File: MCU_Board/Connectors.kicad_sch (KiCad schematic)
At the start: 6 parts, among them J1 Conn_ARM_JTAG_SWD_20, J2 USB_B_Micro, J3 Conn_02x05_Counter_Clockwise

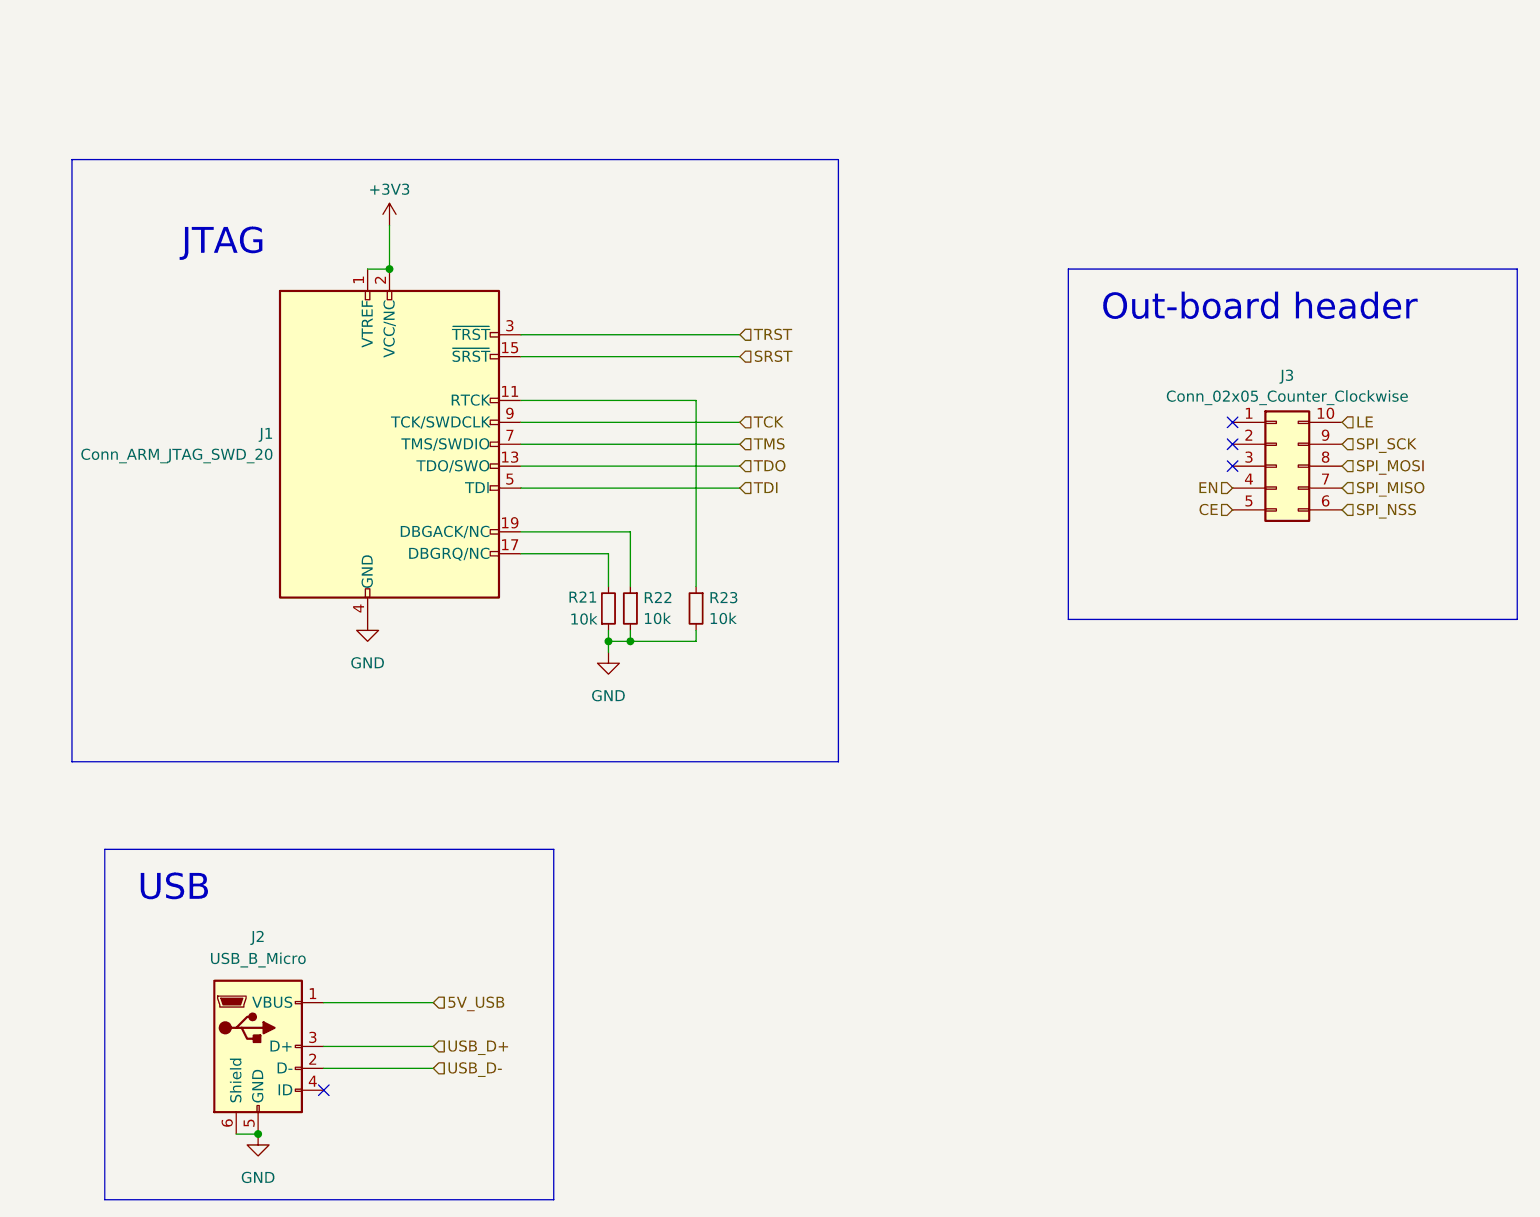
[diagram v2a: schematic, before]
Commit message: Finished MCU board
Finished MCU board and started finishing up the VCO board
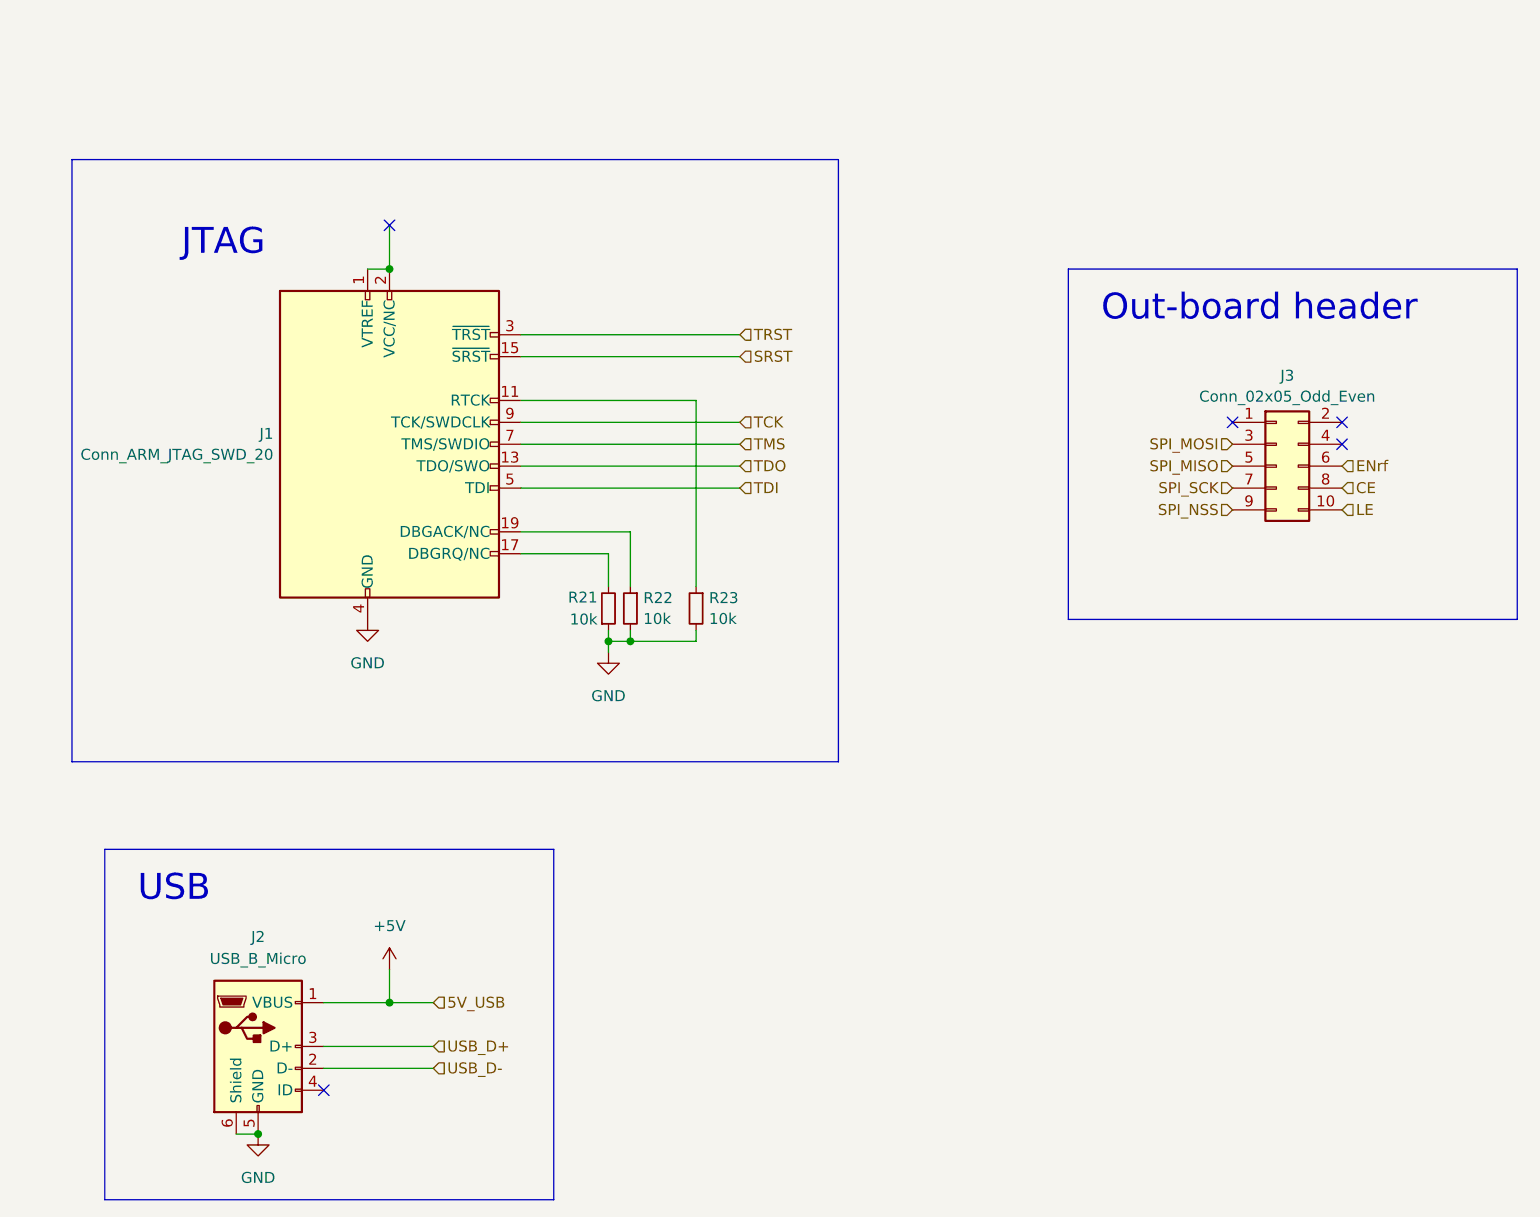
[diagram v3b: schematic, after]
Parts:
- removed J3: Conn_02x05_Counter_Clockwise, Connector_PinHeader_2.54mm:PinHeader_2x05_P2.54mm_Vertical, symbol Connector_Generic:Conn_02x05_Counter_Clockwise
- added J3: Conn_02x05_Odd_Even, Connector_PinHeader_2.54mm:PinHeader_2x05_P2.54mm_Vertical, symbol Connector_Generic:Conn_02x05_Odd_Even
- R21, R22, R23: footprint Resistor_SMD:R_0603_1608Metric_Pad0.98x0.95mm_HandSolder -> Resistor_SMD:R_0402_1005Metric_Pad0.72x0.64mm_HandSolder
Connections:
- net CE: now also J3.8 (Pin_8)
- net LE: now also J3.10 (Pin_10)
- net SPI_MISO: now also J3.5 (Pin_5)
- net SPI_MOSI: now also J3.3 (Pin_3)
- net SPI_NSS: now also J3.9 (Pin_9)
- net SPI_SCK: now also J3.7 (Pin_7)
- net +3V3: no longer names the net of J1.1 (VTREF), J1.2 (VCC/NC)
- net 5V_USB renamed +5V
- new net ENrf: J3.6 (Pin_6)
- no-connect marks 4 -> 5
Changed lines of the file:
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@@
   (junction (at 64.77 148.59) (diameter 0) (color 0 0 0 0)
   )
+  (junction (at 80.01 133.35) (diameter 0) (color 0 0 0 0)
+  )
   (junction (at 107.95 91.44) (diameter 0) (color 0 0 0 0)
   )
   (junction (at 80.01 48.26) (diameter 0) (color 0 0 0 0)
   )
-  (no_connect (at 177.8 71.12))
+  (no_connect (at 190.5 66.04))
+  (no_connect (at 190.5 68.58))
+  (no_connect (at 80.01 43.18))
   (no_connect (at 177.8 66.04))
-  (no_connect (at 177.8 68.58))
   (no_connect (at 72.39 143.51))
   (wire (pts (xy 85.09 140.97) (xy 72.39 140.97))
@@
     (stroke (width 0) (type default))
   )
+  (wire (pts (xy 80.01 129.54) (xy 80.01 133.35))
+    (stroke (width 0) (type default))
+  )
   (wire (pts (xy 95.25 63.5) (xy 115.57 63.5))
     (stroke (width 0) (type default))
@@
     (stroke (width 0) (type default))
   )
-  (wire (pts (xy 85.09 133.35) (xy 72.39 133.35))
+  (wire (pts (xy 85.09 133.35) (xy 80.01 133.35))
     (stroke (width 0) (type default))
   )
   (wire (pts (xy 115.57 63.5) (xy 115.57 85.09))
+    (stroke (width 0) (type default))
+  )
+  (wire (pts (xy 80.01 133.35) (xy 72.39 133.35))
     (stroke (width 0) (type default))
   )
@@
     (effects (font (size 3 3)) (justify left bottom))
   )
-  (hierarchical_label "SPI_SCK" (shape input) (at 190.5 68.58 0) (fields_autoplaced)
-    (effects (font (size 1.27 1.27)) (justify left))
-  )
-  (hierarchical_label "SPI_NSS" (shape input) (at 190.5 76.2 0) (fields_autoplaced)
-    (effects (font (size 1.27 1.27)) (justify left))
+  (hierarchical_label "SPI_SCK" (shape input) (at 177.8 73.66 180) (fields_autoplaced)
+    (effects (font (size 1.27 1.27)) (justify right))
+  )
+  (hierarchical_label "SPI_NSS" (shape input) (at 177.8 76.2 180) (fields_autoplaced)
+    (effects (font (size 1.27 1.27)) (justify right))
   )
   (hierarchical_label "USB_D-" (shape input) (at 85.09 140.97 0) (fields_autoplaced)
@@
     (effects (font (size 1.27 1.27)) (justify left))
   )
-  (hierarchical_label "SPI_MOSI" (shape input) (at 190.5 71.12 0) (fields_autoplaced)
-    (effects (font (size 1.27 1.27)) (justify left))
-  )
-  (hierarchical_label "SPI_MISO" (shape input) (at 190.5 73.66 0) (fields_autoplaced)
-    (effects (font (size 1.27 1.27)) (justify left))
-  )
-  (hierarchical_label "EN" (shape input) (at 177.8 73.66 180) (fields_autoplaced)
+  (hierarchical_label "SPI_MOSI" (shape input) (at 177.8 68.58 180) (fields_autoplaced)
     (effects (font (size 1.27 1.27)) (justify right))
   )
-  (hierarchical_label "CE" (shape input) (at 177.8 76.2 180) (fields_autoplaced)
+  (hierarchical_label "SPI_MISO" (shape input) (at 177.8 71.12 180) (fields_autoplaced)
     (effects (font (size 1.27 1.27)) (justify right))
   )
+  (hierarchical_label "ENrf" (shape input) (at 190.5 71.12 0) (fields_autoplaced)
+    (effects (font (size 1.27 1.27)) (justify left))
+  )
+  (hierarchical_label "CE" (shape input) (at 190.5 73.66 0) (fields_autoplaced)
+    (effects (font (size 1.27 1.27)) (justify left))
+  )
   (hierarchical_label "TDO" (shape input) (at 120.65 71.12 0) (fields_autoplaced)
     (effects (font (size 1.27 1.27)) (justify left))
@@
     (effects (font (size 1.27 1.27)) (justify left))
   )
-  (hierarchical_label "LE" (shape input) (at 190.5 66.04 0) (fields_autoplaced)
+  (hierarchical_label "LE" (shape input) (at 190.5 76.2 0) (fields_autoplaced)
     (effects (font (size 1.27 1.27)) (justify left))
   )
@@
       (effects (font (size 1.27 1.27)) (justify right))
     )
-    (property "Footprint" "Resistor_SMD:R_0603_1608Metric_Pad0.98x0.95mm_HandSolder" (at 107.95 87.63 0)
+    (property "Footprint" "Resistor_SMD:R_0402_1005Metric_Pad0.72x0.64mm_HandSolder" (at 107.95 87.63 0)
       (effects (font (size 1.27 1.27)) hide)
     )
@@
       (effects (font (size 1.27 1.27)) (justify right))
     )
-    (property "Footprint" "Resistor_SMD:R_0603_1608Metric_Pad0.98x0.95mm_HandSolder" (at 115.57 87.63 0)
+    (property "Footprint" "Resistor_SMD:R_0402_1005Metric_Pad0.72x0.64mm_HandSolder" (at 115.57 87.63 0)
       (effects (font (size 1.27 1.27)) hide)
     )
@@
     )
   )
+  (symbol (lib_id "power:+5V") (at 80.01 129.54 0) (unit 1)
+    (in_bom yes) (on_board yes) (dnp no) (fields_autoplaced)
+    (property "Reference" "#PWR040" (at 80.01 133.35 0)
+      (effects (font (size 1.27 1.27)) hide)
+    )
+    (property "Value" "+5V" (at 80.01 124.46 0)
+      (effects (font (size 1.27 1.27)))
+    )
+    (property "Footprint" "" (at 80.01 129.54 0)
+      (effects (font (size 1.27 1.27)) hide)
+    )
+    (property "Datasheet" "" (at 80.01 129.54 0)
+      (effects (font (size 1.27 1.27)) hide)
+    )
+    (pin "1")
+    (instances
+      (project "MCU_Board"
+        (path "/29349b68-071c-451b-9b1e-10b5ef7e12a6/fa8fa127-05a9-4ec7-8a64-8bfb966dae3d"
+          (reference "#PWR040") (unit 1)
+        )
+        (path "/29349b68-071c-451b-9b1e-10b5ef7e12a6/e8aaa04a-3e0b-4fcc-9719-a58df410b7e1"
+          (reference "#PWR06") (unit 1)
+        )
+      )
+    )
+  )
   (symbol (lib_id "power:GND") (at 77.47 88.9 0) (unit 1)
     (in_bom yes) (on_board yes) (dnp no)
@@
     )
   )
-  (symbol (lib_id "power:+3V3") (at 80.01 43.18 0) (unit 1)
-    (in_bom yes) (on_board yes) (dnp no) (fields_autoplaced)
-    (property "Reference" "#PWR03" (at 80.01 46.99 0)
-      (effects (font (size 1.27 1.27)) hide)
-    )
-    (property "Value" "+3V3" (at 80.01 39.0469 0)
-      (effects (font (size 1.27 1.27)))
-    )
-    (property "Footprint" "" (at 80.01 43.18 0)
-      (effects (font (size 1.27 1.27)) hide)
-    )
-    (property "Datasheet" "" (at 80.01 43.18 0)
-      (effects (font (size 1.27 1.27)) hide)
-    )
-    (pin "1")
-    (instances
-      (project "MCU_Board"
-        (path "/29349b68-071c-451b-9b1e-10b5ef7e12a6/e8aaa04a-3e0b-4fcc-9719-a58df410b7e1"
-          (reference "#PWR03") (unit 1)
-        )
-      )
-    )
-  )
-  (symbol (lib_id "Device:R_Small") (at 105.41 87.63 0) (mirror x) (unit 1)
-    (in_bom yes) (on_board yes) (dnp no)
-    (property "Reference" "R21" (at 104.14 86.36 0)
-      (effects (font (size 1.27 1.27)) (justify right))
-    )
-    (property "Value" "10k" (at 104.14 88.9 0)
-      (effects (font (size 1.27 1.27)) (justify right))
-    )
-    (property "Footprint" "Resistor_SMD:R_0603_1608Metric_Pad0.98x0.95mm_HandSolder" (at 105.41 87.63 0)
-      (effects (font (size 1.27 1.27)) hide)
-    )
-    (property "Datasheet" "~" (at 105.41 87.63 0)
-      (effects (font (size 1.27 1.27)) hide)
-    )
-    (pin "1")
-    (pin "2")
-    (instances
-      (project "MCU_Board"
-        (path "/29349b68-071c-451b-9b1e-10b5ef7e12a6/e8aaa04a-3e0b-4fcc-9719-a58df410b7e1"
-          (reference "R21") (unit 1)
-        )
-      )
-    )
-  )
-  (symbol (lib_id "Connector_Generic:Conn_02x05_Counter_Clockwise") (at 182.88 71.12 0) (unit 1)
+  (symbol (lib_id "Connector_Generic:Conn_02x05_Odd_Even") (at 182.88 71.12 0) (unit 1)
     (in_bom yes) (on_board yes) (dnp no) (fields_autoplaced)
     (property "Reference" "J3" (at 184.15 60.6257 0)
       (effects (font (size 1.27 1.27)))
     )
-    (property "Value" "Conn_02x05_Counter_Clockwise" (at 184.15 63.0499 0)
+    (property "Value" "Conn_02x05_Odd_Even" (at 184.15 63.0499 0)
       (effects (font (size 1.27 1.27)))
     )
@@
         )
       )
+    )
+  )
+  (symbol (lib_id "Device:R_Small") (at 105.41 87.63 0) (mirror x) (unit 1)
+    (in_bom yes) (on_board yes) (dnp no)
+    (property "Reference" "R21" (at 104.14 86.36 0)
+      (effects (font (size 1.27 1.27)) (justify right))
+    )
+    (property "Value" "10k" (at 104.14 88.9 0)
+      (effects (font (size 1.27 1.27)) (justify right))
+    )
+    (property "Footprint" "Resistor_SMD:R_0402_1005Metric_Pad0.72x0.64mm_HandSolder" (at 105.41 87.63 0)
+      (effects (font (size 1.27 1.27)) hide)
+    )
+    (property "Datasheet" "~" (at 105.41 87.63 0)
+      (effects (font (size 1.27 1.27)) hide)
+    )
+    (pin "1")
+    (pin "2")
+    (instances
+      (project "MCU_Board"
+        (path "/29349b68-071c-451b-9b1e-10b5ef7e12a6/e8aaa04a-3e0b-4fcc-9719-a58df410b7e1"
+          (reference "R21") (unit 1)
+        )
+      )
